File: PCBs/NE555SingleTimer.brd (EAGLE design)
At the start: 22 x 32 mm, 5 parts, among them IC1 LM555N

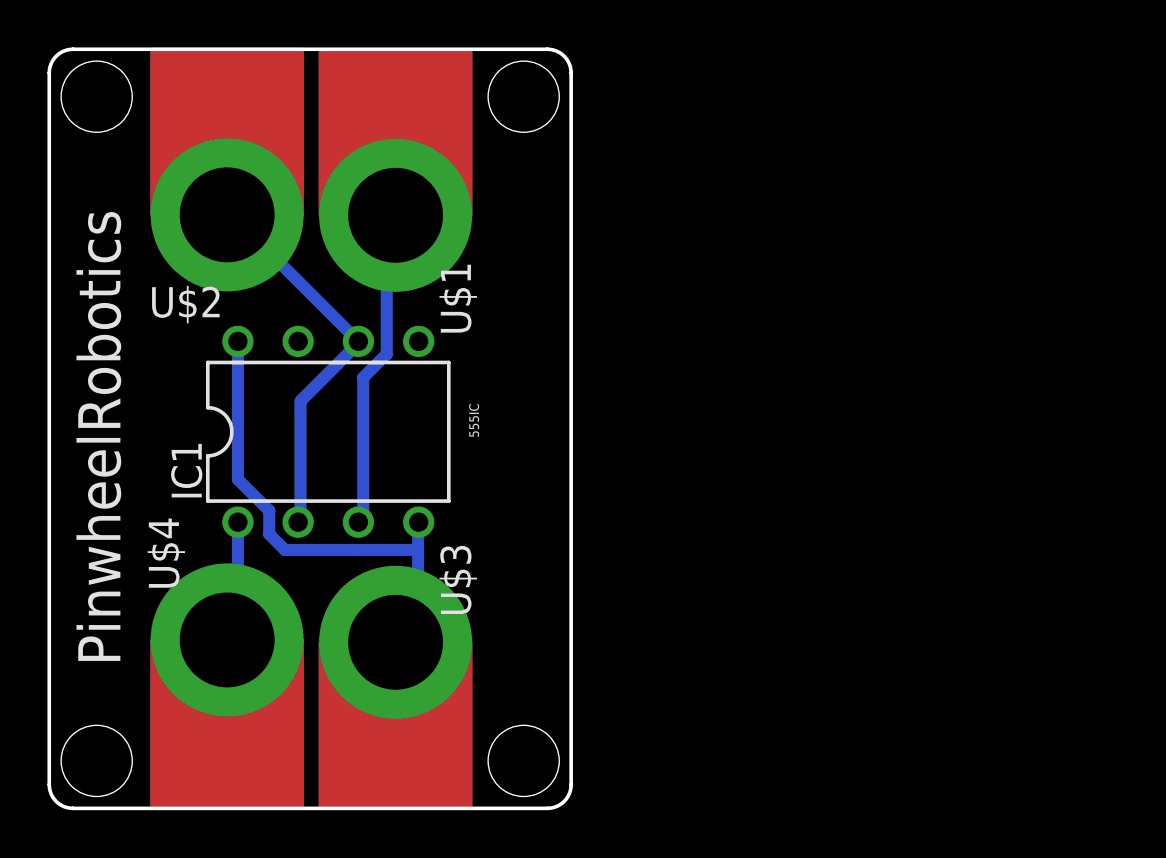
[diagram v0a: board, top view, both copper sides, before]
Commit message: Update for Dim width is 42 length is 28 for type 2 pcb
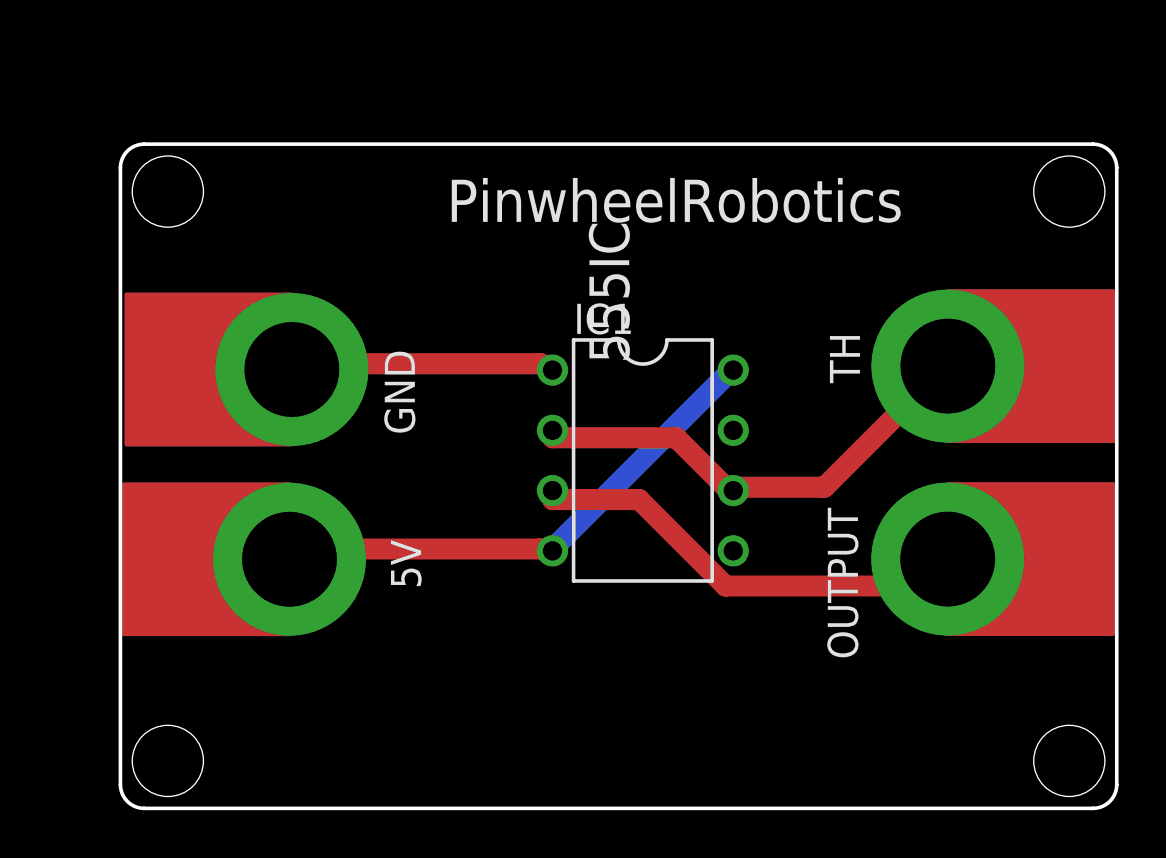
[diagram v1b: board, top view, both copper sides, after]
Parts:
- removed U$1, U$2, U$3, U$4: MICROBIT_PAD, microbit:MICROBIT_PAD
- added 5V, GND, OUTPUT, TH: MICROBIT_PAD, microbit:MICROBIT_PAD
- moved IC1 13.3 mm to (22.0, 14.7), turned to 270 degrees
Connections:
- net 5V: now also 5V.PAD; no longer U$3.PAD
- net GND: now also GND.PAD; no longer U$4.PAD
- net N$1: now also OUTPUT.PAD; no longer U$1.PAD
- net N$2: now also TH.PAD; no longer U$2.PAD
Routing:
- net GND: track 5.13 -> 11.2 mm
- net N$1: track 13.7 -> 19.0 mm
- net N$2: track 16.4 -> 20.0 mm
- net 5V: track 20.8 -> 22.2 mm
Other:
- board size 22 x 32 mm -> 42 x 28 mm
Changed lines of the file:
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@@
 <drawing>
 <settings>
-<setting alwaysvectorfont="no"/>
+<setting alwaysvectorfont="yes"/>
 <setting verticaltext="up"/>
 </settings>
@@
 <board>
 <plain>
-<text x="15.113" y="15.621" size="0.4064" layer="21" rot="R90">555IC</text>
-<wire x1="18" y1="32" x2="-2" y2="32" width="0.1524" layer="20"/>
-<wire x1="-2" y1="32" x2="-3" y2="31" width="0.1524" layer="20" curve="90"/>
-<wire x1="-3" y1="31" x2="-3" y2="1" width="0.1524" layer="20"/>
-<wire x1="-3" y1="1" x2="-2" y2="0" width="0.1524" layer="20" curve="90"/>
-<wire x1="-2" y1="0" x2="18" y2="0" width="0.1524" layer="20"/>
-<wire x1="18" y1="0" x2="19" y2="1" width="0.1524" layer="20" curve="90"/>
-<wire x1="19" y1="1" x2="19" y2="31" width="0.1524" layer="20"/>
-<wire x1="19" y1="31" x2="18" y2="32" width="0.1524" layer="20" curve="90"/>
-<hole x="-1" y="30" drill="3"/>
-<hole x="17" y="30" drill="3"/>
-<hole x="17" y="2" drill="3"/>
-<hole x="-1" y="2" drill="3"/>
-<text x="0" y="6" size="1.778" layer="21" rot="R90">PinwheelRobotics </text>
-<text x="18.5" y="25" size="1.778" layer="22" rot="MR270">care@pinwheel</text>
-<dimension x1="-4.5" y1="32" x2="-4.5" y2="0" x3="-7.5" y3="16" textsize="1.778" layer="1"/>
-<dimension x1="-3" y1="32.5" x2="19" y2="32.5" x3="8" y3="34.5" textsize="1.778" layer="1"/>
+<text x="21.447" y="18.748" size="1.6764" layer="21" rot="R90">555IC</text>
+<wire x1="0" y1="27" x2="0" y2="1" width="0.1524" layer="20"/>
+<wire x1="0" y1="1" x2="1" y2="0" width="0.1524" layer="20" curve="90"/>
+<wire x1="1" y1="0" x2="41" y2="0" width="0.1524" layer="20"/>
+<wire x1="41" y1="0" x2="42" y2="1" width="0.1524" layer="20" curve="90"/>
+<wire x1="42" y1="1" x2="42" y2="27" width="0.1524" layer="20"/>
+<wire x1="42" y1="27" x2="41" y2="28" width="0.1524" layer="20" curve="90"/>
+<wire x1="41" y1="28" x2="1" y2="28" width="0.1524" layer="20"/>
+<wire x1="1" y1="28" x2="0" y2="27" width="0.1524" layer="20" curve="90"/>
+<hole x="2" y="26" drill="3"/>
+<hole x="40" y="26" drill="3"/>
+<hole x="40" y="2" drill="3"/>
+<hole x="2" y="2" drill="3"/>
+<text x="33" y="26.5" size="1.778" layer="21" rot="R180">PinwheelRobotics </text>
+<text x="13.723" y="3.873" size="1.778" layer="22" rot="MR180">care@pinwheel</text>
 </plain>
 <attributes>
@@
 <param name="mdDrill" value="6mil"/>
 <param name="mdSmdStop" value="0mil"/>
-<param name="msWidth" value="20mil"/>
+<param name="msWidth" value="35mil"/>
 <param name="msDrill" value="0.35mm"/>
 <param name="msMicroVia" value="9.99mm"/>
@@
 <param name="TopRouterVariant" value="1"/>
 <param name="tpViaShape" value="round"/>
-<param name="PrefDir.1" value="0"/>
+<param name="PrefDir.1" value="a"/>
 <param name="PrefDir.2" value="0"/>
 <param name="PrefDir.3" value="0"/>
@@
 </autorouter>
 <elements>
-<element name="IC1" library="linear" library_urn="urn:adsk.eagle:library:262" package="DIL08" package3d_urn="urn:adsk.eagle:package:16409/2" value="LM555N" x="8.763" y="15.875" smashed="yes">
-<attribute name="NAME" x="3.429" y="12.954" size="1.27" layer="25" ratio="10" rot="R90"/>
-<attribute name="POPULARITY" value="0" x="27.813" y="-20.955" size="1.778" layer="27" display="off"/>
-<attribute name="VALUE" x="5.207" y="15.24" size="1.27" layer="27" ratio="10"/>
+<element name="IC1" library="linear" library_urn="urn:adsk.eagle:library:262" package="DIL08" package3d_urn="urn:adsk.eagle:package:16409/2" value="LM555N" x="22.024" y="14.665" smashed="yes" rot="R270">
+<attribute name="NAME" x="19.103" y="19.999" size="1.27" layer="25" ratio="10"/>
+<attribute name="POPULARITY" value="0" x="-14.806" y="-4.385" size="1.778" layer="27" rot="R270" display="off"/>
+<attribute name="VALUE" x="21.389" y="18.221" size="1.27" layer="27" ratio="10" rot="R270"/>
 </element>
-<element name="U$1" library="microbit" package="MICROBIT_PAD" value="MICROBIT_PAD" x="11.6" y="25" smashed="yes" rot="R180">
-<attribute name="NAME" x="14.775" y="19.92" size="1.27" layer="21" rot="R90"/>
+<element name="OUTPUT" library="microbit" package="MICROBIT_PAD" value="MICROBIT_PAD" x="34.873" y="10.508" smashed="yes" rot="R90">
+<attribute name="NAME" x="31.089" y="6.279" size="1.27" layer="21" rot="R90"/>
 </element>
-<element name="U$2" library="microbit" package="MICROBIT_PAD" value="MICROBIT_PAD" x="4.5" y="25.019" smashed="yes" rot="R180">
-<attribute name="NAME" x="1.198" y="20.701" size="1.27" layer="21"/>
+<element name="TH" library="microbit" package="MICROBIT_PAD" value="MICROBIT_PAD" x="34.881" y="18.643" smashed="yes" rot="R90">
+<attribute name="NAME" x="29.908" y="20.063" size="1.27" layer="21" rot="R270"/>
 </element>
-<element name="U$3" library="microbit" package="MICROBIT_PAD" value="MICROBIT_PAD" x="11.6" y="7" smashed="yes">
-<attribute name="NAME" x="13.505" y="11.191" size="1.27" layer="21" rot="R270"/>
+<element name="5V" library="microbit" package="MICROBIT_PAD" value="MICROBIT_PAD" x="7.127" y="10.5" smashed="yes" rot="R270">
+<attribute name="NAME" x="11.405" y="11.318" size="1.27" layer="21" rot="R270"/>
 </element>
-<element name="U$4" library="microbit" package="MICROBIT_PAD" value="MICROBIT_PAD" x="4.5" y="7.1" smashed="yes">
-<attribute name="NAME" x="1.198" y="12.307" size="1.27" layer="21" rot="R270"/>
+<element name="GND" library="microbit" package="MICROBIT_PAD" value="MICROBIT_PAD" x="7.227" y="18.5" smashed="yes" rot="R270">
+<attribute name="NAME" x="11.143" y="19.344" size="1.27" layer="21" rot="R270"/>
 </element>
 </elements>
@@
 <contactref element="IC1" pad="8"/>
 <contactref element="IC1" pad="4"/>
-<contactref element="U$3" pad="PAD"/>
-<wire x1="12.5476" y1="7.5946" x2="12.5476" y2="10.8966" width="0.508" layer="16"/>
-<wire x1="12.5476" y1="10.8966" x2="12.5476" y2="11.8872" width="0.508" layer="16"/>
-<wire x1="12.1158" y1="7.1628" x2="12.5476" y2="7.5946" width="0.508" layer="16"/>
-<wire x1="12.5476" y1="11.8872" x2="12.573" y2="12.065" width="0.508" layer="16"/>
-<wire x1="12.1158" y1="7.1628" x2="11.6" y2="7" width="0.508" layer="16"/>
-<wire x1="4.953" y1="13.8684" x2="4.953" y2="19.685" width="0.508" layer="16"/>
-<wire x1="6.2738" y1="12.5476" x2="4.953" y2="13.8684" width="0.508" layer="16"/>
-<wire x1="6.2738" y1="11.557" x2="6.2738" y2="12.5476" width="0.508" layer="16"/>
-<wire x1="6.9342" y1="10.8966" x2="6.2738" y2="11.557" width="0.508" layer="16"/>
-<wire x1="12.5476" y1="10.8966" x2="6.9342" y2="10.8966" width="0.508" layer="16"/>
+<contactref element="5V" pad="PAD"/>
+<wire x1="7.2898" y1="10.9347" x2="17.7038" y2="10.9347" width="0.889" layer="1"/>
+<wire x1="17.7038" y1="10.9347" x2="18.214" y2="10.855" width="0.889" layer="1"/>
+<wire x1="7.2898" y1="10.9347" x2="7.127" y2="10.5" width="0.889" layer="1"/>
+<wire x1="18.2245" y1="10.9347" x2="25.5143" y2="18.2245" width="0.889" layer="16"/>
+<wire x1="25.5143" y1="18.2245" x2="25.834" y2="18.475" width="0.889" layer="16"/>
+<wire x1="18.2245" y1="10.9347" x2="18.214" y2="10.855" width="0.889" layer="16"/>
 </signal>
 <signal name="N$1">
 <contactref element="IC1" pad="3"/>
-<contactref element="U$1" pad="PAD"/>
-<wire x1="10.2362" y1="18.161" x2="10.2362" y2="12.2174" width="0.508" layer="16"/>
-<wire x1="11.2268" y1="19.1516" x2="10.2362" y2="18.161" width="0.508" layer="16"/>
-<wire x1="11.2268" y1="24.1046" x2="11.2268" y2="19.1516" width="0.508" layer="16"/>
-<wire x1="11.746" y1="24.6238" x2="11.2268" y2="24.1046" width="0.508" layer="16"/>
-<wire x1="10.2362" y1="12.2174" x2="10.033" y2="12.065" width="0.508" layer="16"/>
-<wire x1="11.746" y1="24.6238" x2="11.6" y2="25" width="0.508" layer="16"/>
+<contactref element="OUTPUT" pad="PAD"/>
+<wire x1="21.8694" y1="13.0175" x2="18.2245" y2="13.0175" width="0.889" layer="1"/>
+<wire x1="25.5143" y1="9.3726" x2="21.8694" y2="13.0175" width="0.889" layer="1"/>
+<wire x1="33.3248" y1="9.3726" x2="25.5143" y2="9.3726" width="0.889" layer="1"/>
+<wire x1="34.3662" y1="10.414" x2="33.3248" y2="9.3726" width="0.889" layer="1"/>
+<wire x1="18.2245" y1="13.0175" x2="18.214" y2="13.395" width="0.889" layer="1"/>
+<wire x1="34.3662" y1="10.414" x2="34.873" y2="10.508" width="0.889" layer="1"/>
 </signal>
 <signal name="N$2">
 <contactref element="IC1" pad="6"/>
 <contactref element="IC1" pad="2"/>
-<contactref element="U$2" pad="PAD"/>
-<wire x1="7.5946" y1="17.1704" x2="7.5946" y2="12.2174" width="0.508" layer="16"/>
-<wire x1="9.906" y1="19.4818" x2="7.5946" y2="17.1704" width="0.508" layer="16"/>
-<wire x1="7.5946" y1="12.2174" x2="7.493" y2="12.065" width="0.508" layer="16"/>
-<wire x1="9.906" y1="19.4818" x2="10.033" y2="19.685" width="0.508" layer="16"/>
-<wire x1="4.699" y1="25.019" x2="10.033" y2="19.685" width="0.508" layer="16"/>
-<wire x1="4.5" y1="25.019" x2="4.699" y2="25.019" width="0.508" layer="16"/>
+<contactref element="TH" pad="PAD"/>
+<wire x1="23.4315" y1="15.621" x2="18.2245" y2="15.621" width="0.889" layer="1"/>
+<wire x1="25.5143" y1="13.5382" x2="23.4315" y2="15.621" width="0.889" layer="1"/>
+<wire x1="18.2245" y1="15.621" x2="18.214" y2="15.935" width="0.889" layer="1"/>
+<wire x1="25.5143" y1="13.5382" x2="25.834" y2="13.395" width="0.889" layer="1"/>
+<wire x1="29.6799" y1="13.5382" x2="26.035" y2="13.5382" width="0.889" layer="1"/>
+<wire x1="34.3662" y1="18.2245" x2="29.6799" y2="13.5382" width="0.889" layer="1"/>
+<wire x1="26.035" y1="13.5382" x2="25.834" y2="13.395" width="0.889" layer="1"/>
+<wire x1="34.3662" y1="18.2245" x2="34.881" y2="18.643" width="0.889" layer="1"/>
 </signal>
 <signal name="GND">
 <contactref element="IC1" pad="1"/>
-<contactref element="U$4" pad="PAD"/>
-<wire x1="4.953" y1="7.656284375" x2="4.953" y2="12.065" width="0.508" layer="16"/>
-<wire x1="4.953" y1="7.656284375" x2="4.5" y2="7.1" width="0.508" layer="16"/>
+<contactref element="GND" pad="PAD"/>
+<wire x1="7.2898" y1="18.7452" x2="17.7038" y2="18.7452" width="0.889" layer="1"/>
+<wire x1="17.7038" y1="18.7452" x2="18.214" y2="18.475" width="0.889" layer="1"/>
+<wire x1="7.2898" y1="18.7452" x2="7.227" y2="18.5" width="0.889" layer="1"/>
 </signal>
 </signals>
